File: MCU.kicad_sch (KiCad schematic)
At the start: 7 parts, among them U5 ESP32-S3-WROOM-1

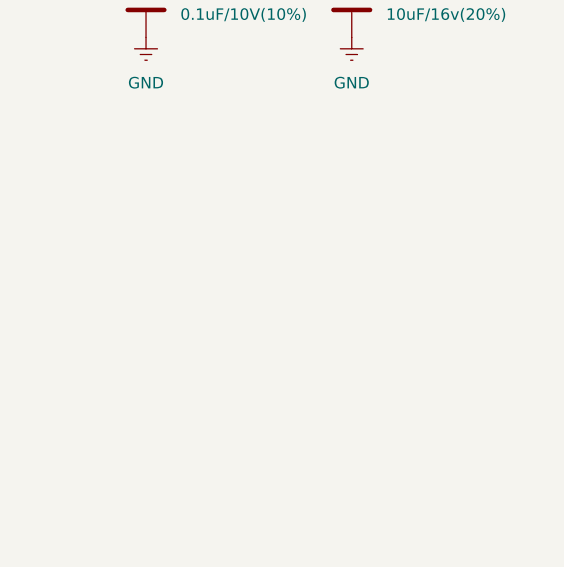
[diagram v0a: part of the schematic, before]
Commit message: Initial population of PCB
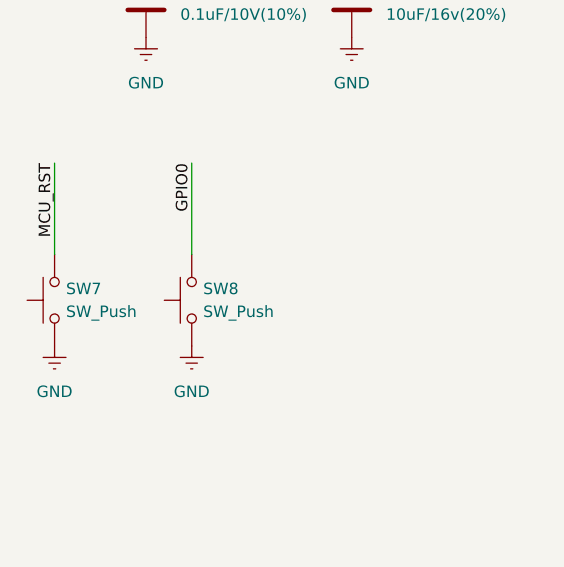
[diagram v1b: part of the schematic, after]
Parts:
- added SW7, SW8: SW_Push, Button_Switch_SMD:SW_SPST_PTS645, symbol Switch:SW_Push
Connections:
- net GND: now also SW7.1, SW8.1
- net GPIO0: now also SW8.2
- net MCU_RST: now also SW7.2

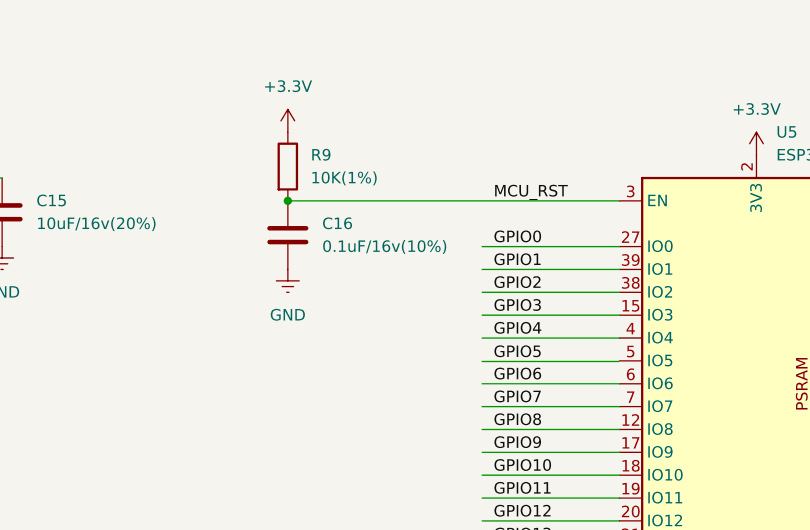
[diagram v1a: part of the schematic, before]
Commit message: Added DSP, Neopixles, MIC's and mounting holes
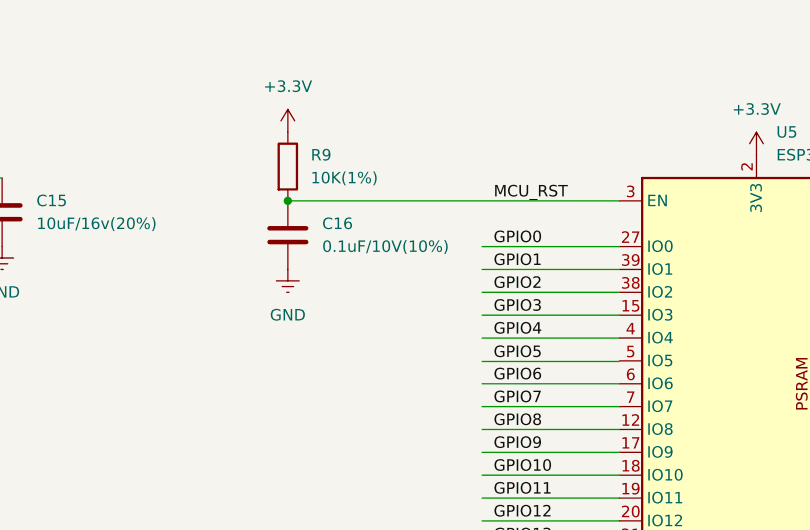
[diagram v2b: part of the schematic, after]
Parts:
- C14, C15: footprint Capacitor_SMD:C_0603_1608Metric -> Capacitor_SMD:C_0402_1005Metric
- C16: value 0.1uF/16v(10%) -> 0.1uF/10V(10%); footprint Capacitor_SMD:C_0603_1608Metric -> Capacitor_SMD:C_0402_1005Metric
- R10, R11, R9: footprint Resistor_SMD:R_0603_1608Metric -> Resistor_SMD:R_0402_1005Metric
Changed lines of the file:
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@@
 			)
 		)
-		(property "Footprint" "Resistor_SMD:R_0603_1608Metric"
+		(property "Footprint" "Resistor_SMD:R_0402_1005Metric"
 			(at 252.222 26.67 90)
 			(effects
@@
 			)
 		)
-		(property "Footprint" "Resistor_SMD:R_0603_1608Metric"
+		(property "Footprint" "Resistor_SMD:R_0402_1005Metric"
 			(at 266.192 26.67 90)
 			(effects
@@
 			)
 		)
-		(property "Footprint" "Capacitor_SMD:C_0603_1608Metric"
+		(property "Footprint" "Capacitor_SMD:C_0402_1005Metric"
 			(at 33.9852 39.37 0)
 			(effects
@@
 			)
 		)
-		(property "Footprint" "Capacitor_SMD:C_0603_1608Metric"
+		(property "Footprint" "Capacitor_SMD:C_0402_1005Metric"
 			(at 56.8452 39.37 0)
 			(effects
@@
 			)
 		)
-		(property "Value" "0.1uF/16v(10%)"
+		(property "Value" "0.1uF/10V(10%)"
 			(at 91.44 39.3699 0)
 			(effects
@@
 			)
 		)
-		(property "Footprint" "Capacitor_SMD:C_0603_1608Metric"
+		(property "Footprint" "Capacitor_SMD:C_0402_1005Metric"
 			(at 88.5952 41.91 0)
 			(effects
@@
 			)
 		)
-		(property "Footprint" "Resistor_SMD:R_0603_1608Metric"
+		(property "Footprint" "Resistor_SMD:R_0402_1005Metric"
 			(at 85.852 30.48 90)
 			(effects
